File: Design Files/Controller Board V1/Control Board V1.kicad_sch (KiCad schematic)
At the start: 18 parts

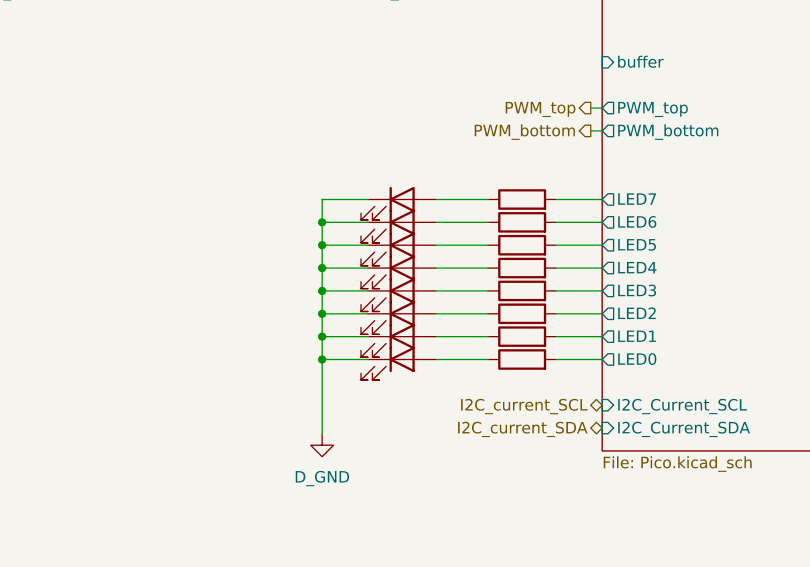
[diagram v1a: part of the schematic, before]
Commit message: Changed to four layer and added pours
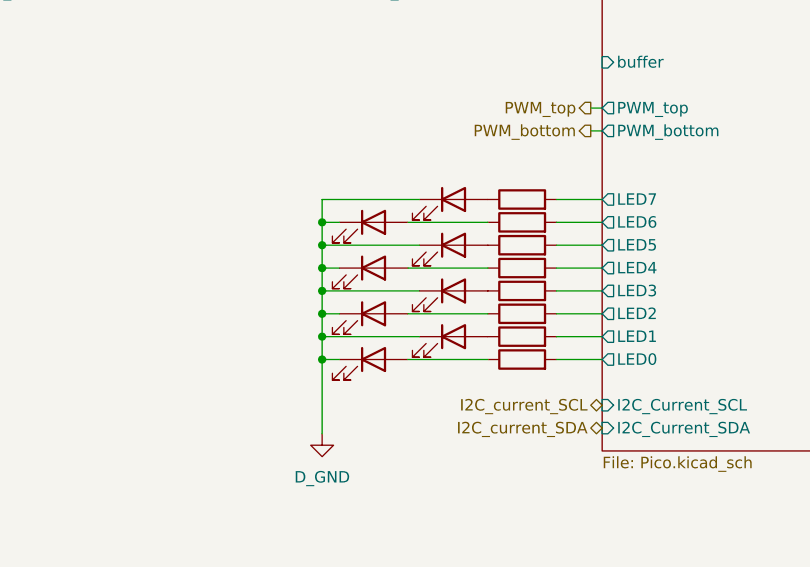
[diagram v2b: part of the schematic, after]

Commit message: Minor Changes
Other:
- sheet Pico ports: added A_GND, D_GND; removed buffer, inv, sig_gnd
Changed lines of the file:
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@@
 		(shape output)
 		(at 135.89 72.39 180)
+		(fields_autoplaced yes)
 		(effects
 			(font
@@
 		(shape input)
 		(at 222.25 87.63 0)
+		(fields_autoplaced yes)
 		(effects
 			(font
@@
 		(shape input)
 		(at 20.32 83.82 180)
+		(fields_autoplaced yes)
 		(effects
 			(font
@@
 		(shape input)
 		(at 97.79 22.86 90)
+		(fields_autoplaced yes)
 		(effects
 			(font
@@
 		(shape input)
 		(at 41.91 45.72 0)
+		(fields_autoplaced yes)
 		(effects
 			(font
@@
 		(shape bidirectional)
 		(at 36.83 90.17 0)
+		(fields_autoplaced yes)
 		(effects
 			(font
@@
 		(shape input)
 		(at 40.64 83.82 0)
+		(fields_autoplaced yes)
 		(effects
 			(font
@@
 		(shape bidirectional)
 		(at 38.1 125.73 0)
+		(fields_autoplaced yes)
 		(effects
 			(font
@@
 		(shape input)
 		(at 110.49 36.83 0)
+		(fields_autoplaced yes)
 		(effects
 			(font
@@
 		(shape bidirectional)
 		(at 36.83 87.63 0)
+		(fields_autoplaced yes)
 		(effects
 			(font
@@
 		(shape input)
 		(at 222.25 92.71 0)
+		(fields_autoplaced yes)
 		(effects
 			(font
@@
 		(shape bidirectional)
 		(at 36.83 49.53 0)
+		(fields_autoplaced yes)
 		(effects
 			(font
@@
 		(shape input)
 		(at 20.32 49.53 180)
+		(fields_autoplaced yes)
 		(effects
 			(font
@@
 		(shape input)
 		(at 76.2 45.72 180)
+		(fields_autoplaced yes)
 		(effects
 			(font
@@
 		(shape input)
 		(at 24.13 118.11 180)
+		(fields_autoplaced yes)
 		(effects
 			(font
@@
 		(shape bidirectional)
 		(at 137.16 105.41 180)
+		(fields_autoplaced yes)
 		(effects
 			(font
@@
 		(shape output)
 		(at 135.89 74.93 180)
+		(fields_autoplaced yes)
 		(effects
 			(font
@@
 		(shape bidirectional)
 		(at 137.16 107.95 180)
+		(fields_autoplaced yes)
 		(effects
 			(font
@@
 		(shape input)
 		(at 195.58 64.77 90)
+		(fields_autoplaced yes)
 		(effects
 			(font
@@
 		(shape output)
 		(at 38.1 118.11 0)
+		(fields_autoplaced yes)
 		(effects
 			(font
@@
 		(shape bidirectional)
 		(at 36.83 53.34 0)
+		(fields_autoplaced yes)
 		(effects
 			(font
@@
 		(shape input)
 		(at 76.2 43.18 180)
+		(fields_autoplaced yes)
 		(effects
 			(font
@@
 		(shape bidirectional)
 		(at 38.1 123.19 0)
+		(fields_autoplaced yes)
 		(effects
 			(font
@@
 		(shape input)
 		(at 20.32 147.32 180)
+		(fields_autoplaced yes)
 		(effects
 			(font
@@
 			)
 		)
-		(property "Value" "3.3V"
+		(property "Value" "5V"
 			(at 21.59 73.66 0)
 			(effects
@@
 			)
 		)
-		(property "Value" "3.3V"
+		(property "Value" "5V"
 			(at 21.59 106.68 0)
 			(effects
@@
 			)
 		)
-		(property "Value" "3.3V"
+		(property "Value" "5V"
 			(at 20.32 40.64 0)
 			(effects
@@
 	)
 	(symbol
+		(lib_id "power:GND")
+		(at 161.29 34.29 180)
+		(unit 1)
+		(exclude_from_sim no)
+		(in_bom yes)
+		(on_board yes)
+		(dnp no)
+		(property "Reference" "#PWR02"
+			(at 161.29 27.94 0)
+			(effects
+				(font
+					(size 1.27 1.27)
+				)
+				(hide yes)
+			)
+		)
+		(property "Value" "D_GND"
+			(at 161.29 29.464 0)
+			(effects
+				(font
+					(size 1.27 1.27)
+				)
+			)
+		)
+		(property "Footprint" ""
+			(at 161.29 34.29 0)
+			(effects
+				(font
+					(size 1.27 1.27)
+				)
+				(hide yes)
+			)
+		)
+		(property "Datasheet" ""
+			(at 161.29 34.29 0)
+			(effects
+				(font
+					(size 1.27 1.27)
+				)
+				(hide yes)
+			)
+		)
+		(property "Description" "Power symbol creates a global label with name \"GND\" , ground"
+			(at 161.29 34.29 0)
+			(effects
+				(font
+					(size 1.27 1.27)
+				)
+				(hide yes)
+			)
+		)
+		(pin "1"
+		)
+		(instances
+			(project "Control Board V1"
+				(path "/e0c606b8-cbb9-4aff-b96c-73876da6ca74"
+					(reference "#PWR02")
+					(unit 1)
+				)
+			)
+		)
+	)
+	(symbol
 		(lib_id "Device:LED")
 		(at 111.76 90.17 0)
@@
 	)
 	(symbol
+		(lib_id "power:GND")
+		(at 168.91 34.29 180)
+		(unit 1)
+		(exclude_from_sim no)
+		(in_bom yes)
+		(on_board yes)
+		(dnp no)
+		(property "Reference" "#PWR03"
+			(at 168.91 27.94 0)
+			(effects
+				(font
+					(size 1.27 1.27)
+				)
+				(hide yes)
+			)
+		)
+		(property "Value" "A_GND"
+			(at 168.91 29.464 0)
+			(effects
+				(font
+					(size 1.27 1.27)
+				)
+			)
+		)
+		(property "Footprint" ""
+			(at 168.91 34.29 0)
+			(effects
+				(font
+					(size 1.27 1.27)
+				)
+				(hide yes)
+			)
+		)
+		(property "Datasheet" ""
+			(at 168.91 34.29 0)
+			(effects
+				(font
+					(size 1.27 1.27)
+				)
+				(hide yes)
+			)
+		)
+		(property "Description" "Power symbol creates a global label with name \"GND\" , ground"
+			(at 168.91 34.29 0)
+			(effects
+				(font
+					(size 1.27 1.27)
+				)
+				(hide yes)
+			)
+		)
+		(pin "1"
+		)
+		(instances
+			(project "Control Board V1"
+				(path "/e0c606b8-cbb9-4aff-b96c-73876da6ca74"
+					(reference "#PWR03")
+					(unit 1)
+				)
+			)
+		)
+	)
+	(symbol
 		(lib_id "Device:LED")
 		(at 120.65 92.71 0)
@@
 			)
 		)
-		(pin "sig_gnd" input
-			(at 137.16 38.1 180)
-			(effects
-				(font
-					(size 1.27 1.27)
-				)
-				(justify left)
-			)
-		)
-		(pin "inv" input
-			(at 137.16 44.45 180)
-			(effects
-				(font
-					(size 1.27 1.27)
-				)
-				(justify left)
-			)
-		)
 		(pin "LED7" output
 			(at 137.16 82.55 180)
@@
 			)
 		)
-		(pin "buffer" input
-			(at 137.16 67.31 180)
-			(effects
-				(font
-					(size 1.27 1.27)
-				)
-				(justify left)
-			)
-		)
 		(pin "GPIO_2" bidirectional
 			(at 177.8 97.79 0)
@@
 			)
 		)
+		(pin "D_GND" output
+			(at 161.29 34.29 90)
+			(effects
+				(font
+					(size 1.27 1.27)
+				)
+				(justify right)
+			)
+		)
+		(pin "A_GND" output
+			(at 168.91 34.29 90)
+			(effects
+				(font
+					(size 1.27 1.27)
+				)
+				(justify right)
+			)
+		)

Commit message: OOps, pushing late
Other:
- sheet IO ports: added none; removed GND_IN_PMM
- sheet current_sensor1 ports: added 5V; removed 3V3
- sheet current_sensor2 ports: added 5V; removed 3V3
- sheet current_sensor3 ports: added 5V; removed 3V3
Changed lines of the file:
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@@
-			)
-		)
-		(pin "3V3" input
-			(at 24.13 111.76 180)
-			(effects
-				(font
-					(size 1.27 1.27)
-				)
-				(justify left)
 			)
 		)
@@
 				)
 				(justify right)
+			)
+		)
+		(pin "5V" input
+			(at 24.13 111.76 180)
+			(effects
+				(font
+					(size 1.27 1.27)
+				)
+				(justify left)
 			)
 		)
@@
 			)
 		)
-		(pin "GND_IN_PMM" input
-			(at 217.17 97.79 0)
-			(effects
-				(font
-					(size 1.27 1.27)
-				)
-				(justify right)
-			)
-		)
 		(pin "CAP_IN" input
 			(at 217.17 87.63 0)
@@
 			)
 		)
-		(pin "3V3" input
-			(at 24.13 45.72 180)
-			(effects
-				(font
-					(size 1.27 1.27)
-				)
-				(justify left)
-			)
-		)
 		(pin "VIN+" bidirectional
 			(at 24.13 49.53 180)
@@
 				)
 				(justify right)
+			)
+		)
+		(pin "5V" input
+			(at 24.13 45.72 180)
+			(effects
+				(font
+					(size 1.27 1.27)
+				)
+				(justify left)
 			)
 		)
@@
 			)
 		)
-		(pin "3V3" input
-			(at 24.13 78.74 180)
-			(effects
-				(font
-					(size 1.27 1.27)
-				)
-				(justify left)
-			)
-		)
 		(pin "VIN-" bidirectional
 			(at 36.83 83.82 0)
@@
 			)
 		)
+		(pin "5V" input
+			(at 24.13 78.74 180)
+			(effects
+				(font
+					(size 1.27 1.27)
+				)
+				(justify left)
+			)
+		)

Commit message: board
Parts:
- removed R16, R17: 0, Resistor_SMD:R_0603_1608Metric, symbol Device:R
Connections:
- net D_GND is gone; now on net A_GND: D1.1 (K), D2.1 (K), D3.1 (K), D4.1 (K), D5.1 (K), D6.1 (K), D7.1 (K), D8.1 (K)

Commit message: half finished with brooks changes
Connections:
- net A_GND renamed D_GND

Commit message: changes
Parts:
- R23: value R -> 110
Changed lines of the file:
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@@
 			)
 		)
-		(property "Value" "R"
+		(property "Value" "110"
 			(at 128.27 78.74 90)
 			(effects
